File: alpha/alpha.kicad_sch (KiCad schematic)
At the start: 2 parts, among them M1 Motor_AC_3_phase

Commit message: add power circuitry
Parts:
- added C1: 2200uF, 50V, symbol Device:C
- added J1, J2: Conn_01x02, symbol Connector_Generic:Conn_01x02
- added J10, J3, J4, J5, J6, J7, J8, J9: Conn_01x03, symbol Connector_Generic:Conn_01x03
- added M2, M3, M4: Motor_AC_3_phase, symbol Motors:Motor_AC_3_phase
- added U1: Holybro Pixhawk 6X, symbol Flight_Controllers:Holybro_Pixhawk_6X
- added U2: Holybro PM08D Power Module, symbol Power_Modules:Holybro_PM08D_Power_Module
- added U3: Holybro Tekko32 F4 Metal 4in1 65A ESC, symbol ESCs:Tekko32_F4_Metal_4in1_65A_ESC
- added U4: iFlight Anti Spark Filter, symbol Misc:iFlight_Anti_Spark_Filter
- added U5: RFD868x, symbol RF_Modules:RFD868x-EU_868Mhz_Long_Range
- BT1: value Battery -> Battery 6S
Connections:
- net at BT1.1 (+): now also J1.1 (Pin_1)
- net at BT1.2 (-): now also J1.2 (Pin_2)
- net at M1.1: now also J7.1 (Pin_1)
- net at M1.2: now also J7.2 (Pin_2)
- net at M1.3: now also J7.3 (Pin_3)
- new net: J5.1 (Pin_1), U3. (VBAT)
- new net: J5.2 (Pin_2), U3. (VBAT)
- new net: J5.3 (Pin_3), U3. (VBAT)
- new net: J9.1 (Pin_1), M3.1
- new net: J9.2 (Pin_2), M3.2
- new net: J9.3 (Pin_3), M3.3
- new net: U1. (USB-C), U2. (POWER2) (x2)
- new net: J8.1 (Pin_1), M2.1
- new net: J8.2 (Pin_2), M2.2
- new net: J8.3 (Pin_3), M2.3
- new net: C1.1, U2. (POWER2), U3. (VBAT)
- new net: C1.2, U2. (POWER2), U3. (VBAT)
- new net: J2.2 (Pin_2), U4. (V+)
- new net: U2. (POWER2), U4. (V+)
- new net: J10.1 (Pin_1), M4.1
- new net: J10.2 (Pin_2), M4.2
- new net: J10.3 (Pin_3), M4.3
- new net: J3.1 (Pin_1), U3. (VBAT)
- new net: J3.2 (Pin_2), U3. (VBAT)
- new net: J3.3 (Pin_3), U3. (VBAT)
- new net: J4.1 (Pin_1), U3. (VBAT)
- new net: J4.2 (Pin_2), U3. (VBAT)
- new net: J4.3 (Pin_3), U3. (VBAT)
- new net: J6.1 (Pin_1), U3. (VBAT)
- new net: J6.2 (Pin_2), U3. (VBAT)
- new net: J6.3 (Pin_3), U3. (VBAT)
- new net ESC_TEL: U1. (USB-C), U3. (VBAT)
- new net PWM_MOTORS: U1. (USB-C), U3. (VBAT)
- no-connect marks 0 -> 2
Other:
- note added: "18 AWG"
- note added: "6 AWG"
- note added: "AS150"
- note added: "ESC"
- note added: "FUSE 200A"
- note added: "Flight controller"
- note added: "MT30-MAMASS"
- note added: "POWER1 has I2C sensor output"
- note added: "Redundant supply"
- moved on the sheet: BT1

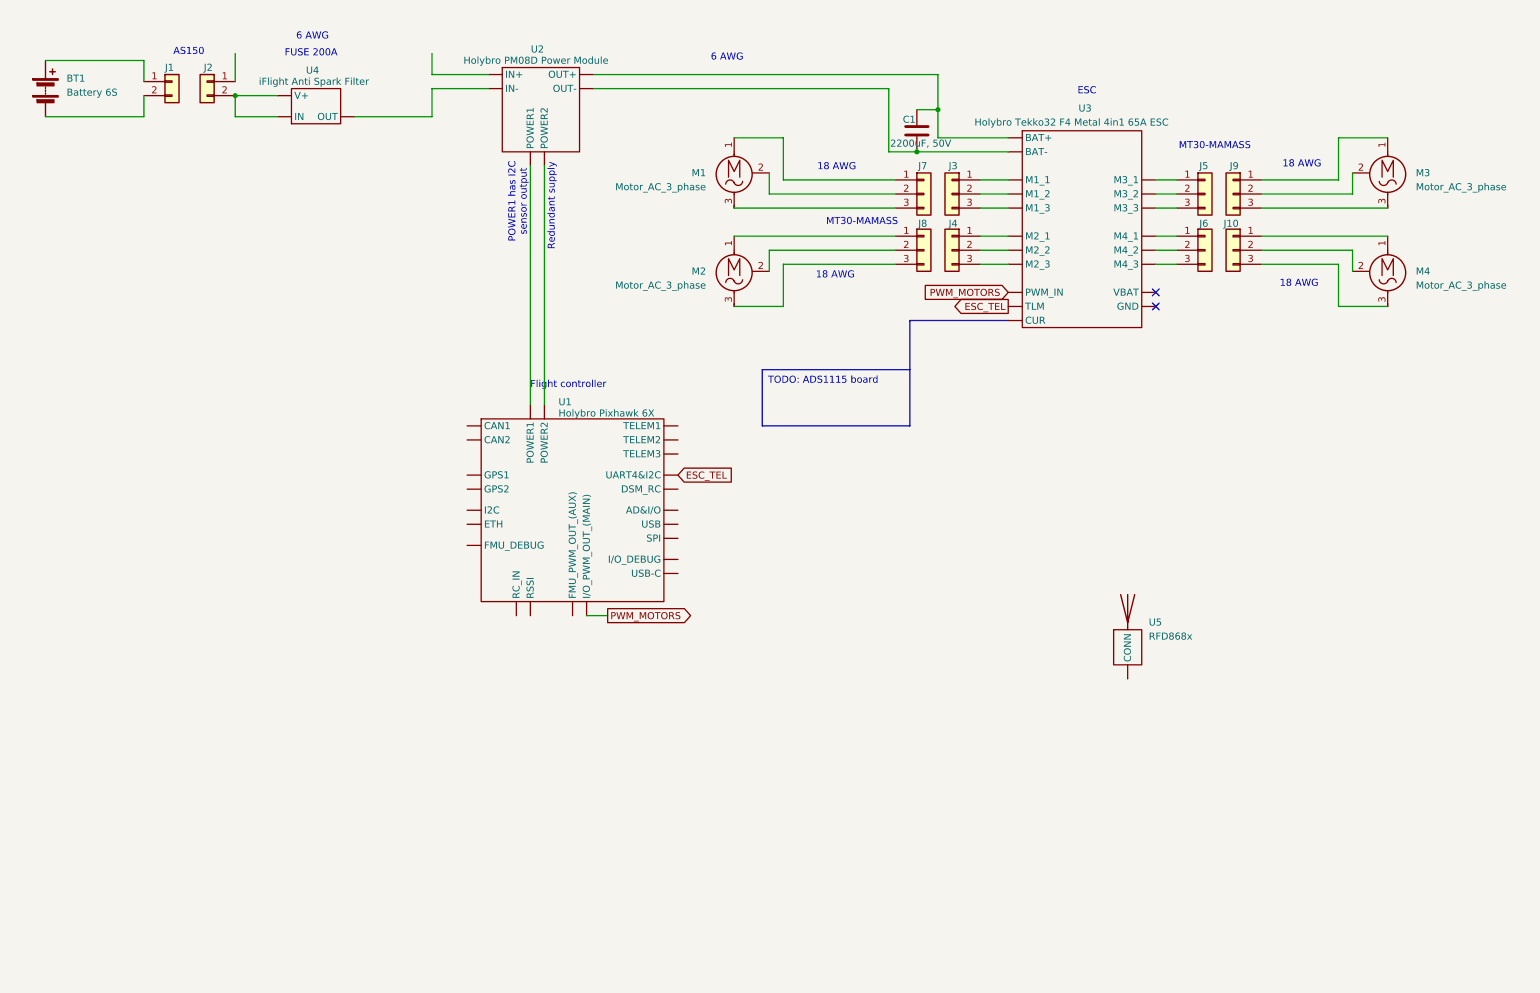
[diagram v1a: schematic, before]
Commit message: Add missing components to schematic
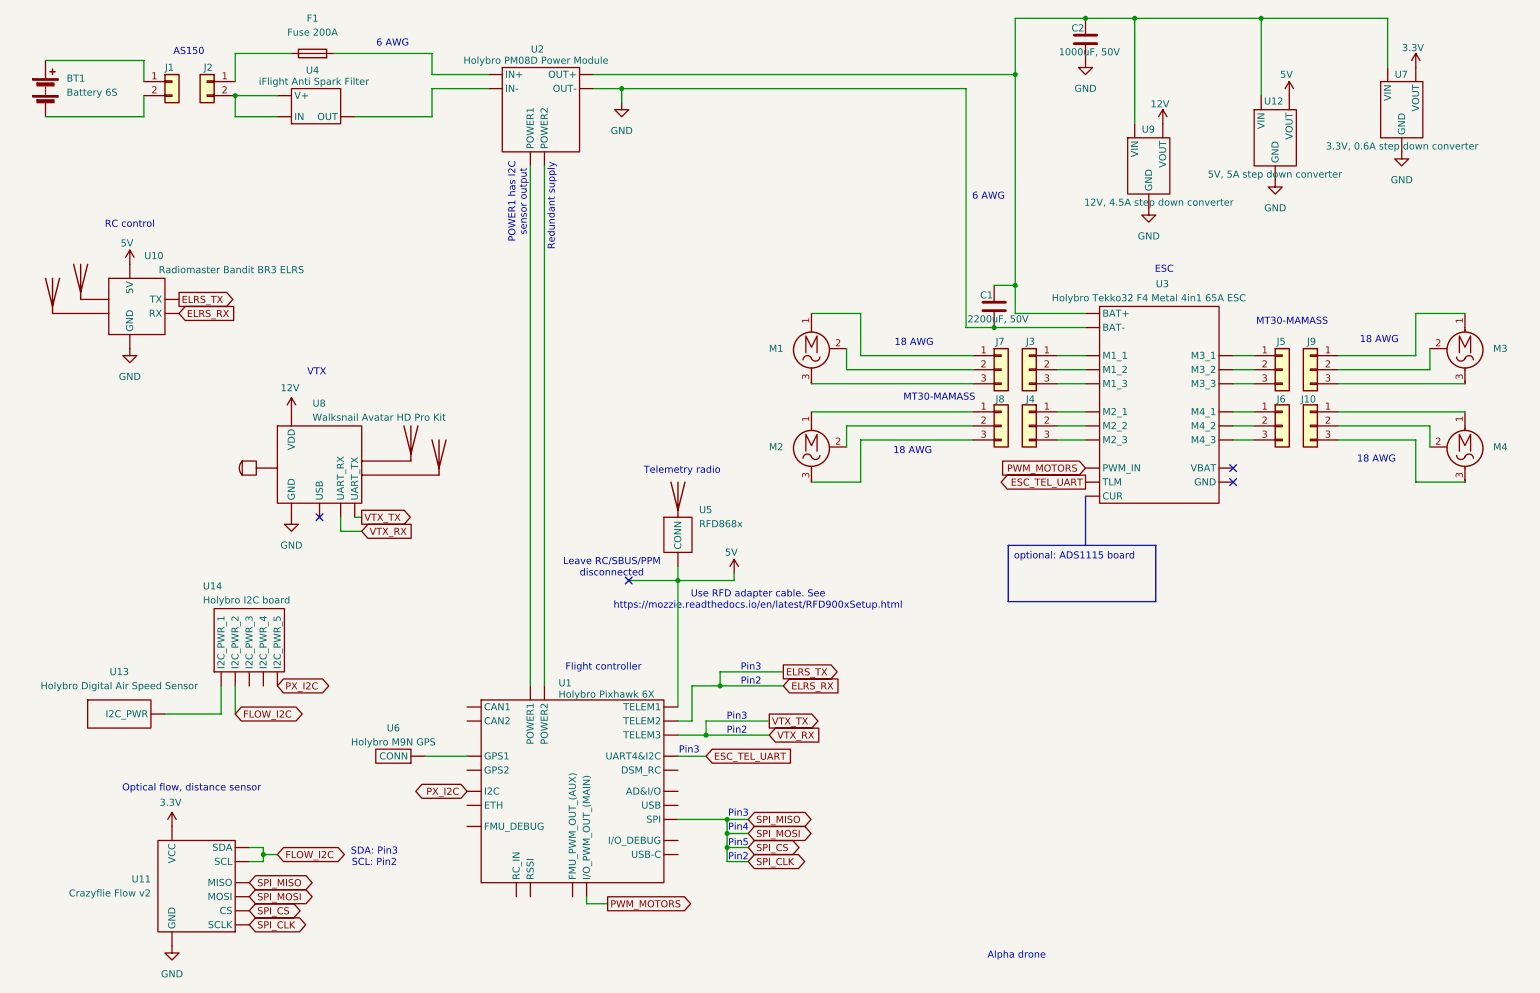
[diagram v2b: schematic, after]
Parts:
- added C2: 1000uF, 50V, symbol Device:C
- added F1: Fuse 200A, symbol Device:Fuse
- added U10: Radiomaster Bandit BR3 ELRS, symbol RF_Modules:Radiomaster_Bandit_BR3_ELRS
- added U11: Crazyflie Flow v2, symbol Sensors:Crazyflie_Flow_v2
- added U12: 5V, 5A step down converter, symbol DC_DC_Converters:DC/DC_Converter
- added U13: Holybro Digital Air Speed Sensor, symbol Sensors:Holybro_Digital_Air_Speed_Sensor
- added U14: Holybro I2C board, symbol Misc:Holybro_I2C_Board
- added U6: Holybro M9N GPS, symbol GPS_Modules:Holybro_M9N_GPS
- added U7: 3.3V, 0.6A step down converter, symbol DC_DC_Converters:DC/DC_Converter
- added U8: Walksnail Avatar HD Pro Kit, symbol Camera_VTX:Walksnail_Avatar_HD_Pro_Kit
- added U9: 12V, 4.5A step down converter, symbol DC_DC_Converters:DC/DC_Converter
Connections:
- net VTX_RX: now reaches U1. (USB-C)
- net VTX_RX: now also U8. (VDD)
- net GND: now reaches U2. (POWER2)
- net GND: now also C1.2, U3. (VBAT), C2.2, U10. (TX), U11. (VCC), U12. (VOUT), U7. (VOUT), U8. (VDD), U9. (VOUT); no longer U1. (USB-C)
- net at J2.1 (Pin_1): now also F1.1
- net 5V: now reaches U5. (CONN)
- net 5V: now also U1. (USB-C), U10. (TX), U12. (VOUT)
- removed net ESC_TEL: U1. (USB-C), U3. (VBAT)
- new net: U1. (USB-C), U2. (POWER2) (x2)
- new net: U1. (USB-C), U6. (CONN)
- new net: C1.1, C2.1, U12. (VOUT), U2. (POWER2), U3. (VBAT), U7. (VOUT), U9. (VOUT)
- new net: U13. (I2C_PWR), U14. (I2C_PWR_5)
- new net: F1.2, U2. (POWER2)
- new net 12V: U8. (VDD), U9. (VOUT)
- new net 3.3V: U11. (VCC), U7. (VOUT)
- new net ELRS_RX: U1. (USB-C), U10. (TX)
- new net ESC_TEL_UART: U1. (USB-C), U3. (VBAT)
- new net FLOW_I2C: U11. (VCC), U14. (I2C_PWR_5)
- new net PX_I2C: U1. (USB-C), U14. (I2C_PWR_5)
- new net SPI_CLK: U1. (USB-C), U11. (VCC)
- no-connect marks 2 -> 4
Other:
- note added: "Alpha drone"
- note added: "Leave RC/SBUS/PPM disconnected"
- note added: "Optical flow, distance sensor"
- note added: "Pin2"
- note added: "Pin3"
- note added: "Pin4"
- note added: "Pin5"
- note added: "RC control"
- note added: "SDA: Pin3 SCL: Pin2"
- note added: "Telemetry radio"
- note added: "Use RFD adapter cable. See https://mozzie.readthedocs.io/en/latest/RFD900xSetup.html"
- note added: "VTX"
- note removed: "FUSE 200A"
- moved on the sheet: C1, J10, J3, J4, J5, J6, J7, J8, J9, M1, M2, M3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

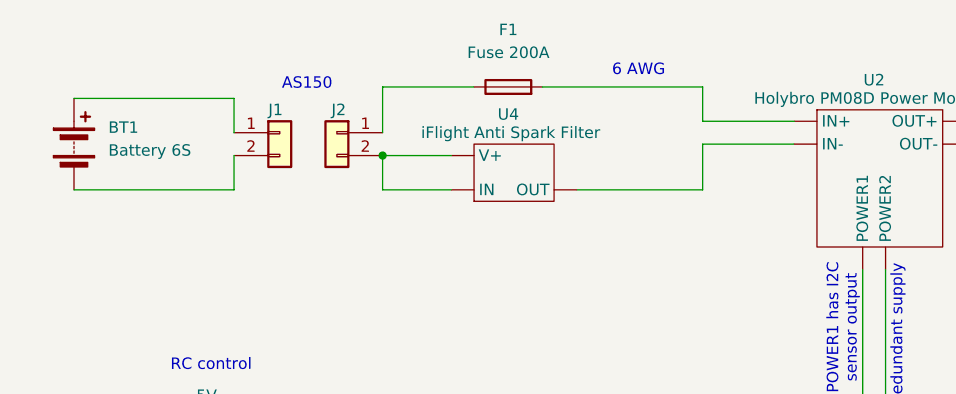
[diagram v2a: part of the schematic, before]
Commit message: fix anti spark filter
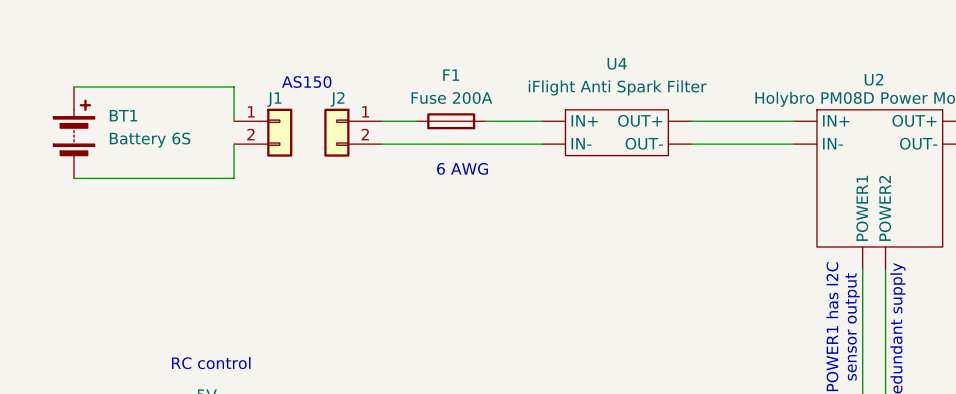
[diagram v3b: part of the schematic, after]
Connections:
- net at U4. (OUT-): now also F1.2; no longer U2. (POWER2)
- new net: U1. (USB-C), U2. (POWER2) (x2)
- new net: C1.1, C2.1, U12. (VOUT), U2. (POWER2), U3. (VBAT), U7. (VOUT), U9. (VOUT)
- new net: U2. (POWER2), U4. (OUT-) (x2)
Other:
- moved on the sheet: BT1, F1, J1, J2

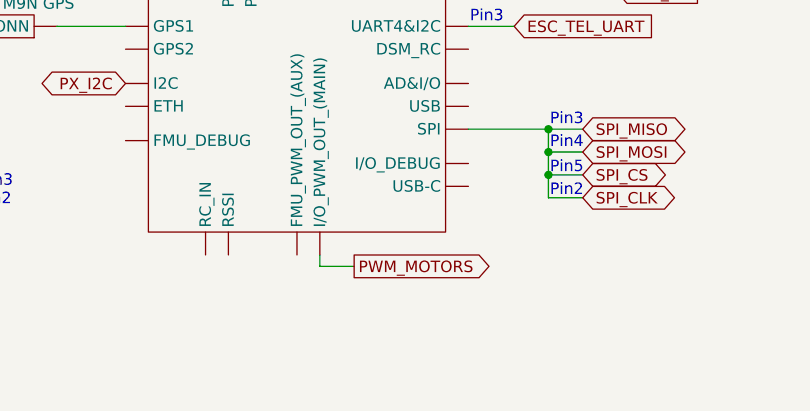
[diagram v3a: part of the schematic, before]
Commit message: assign motors to ports supporting dshot
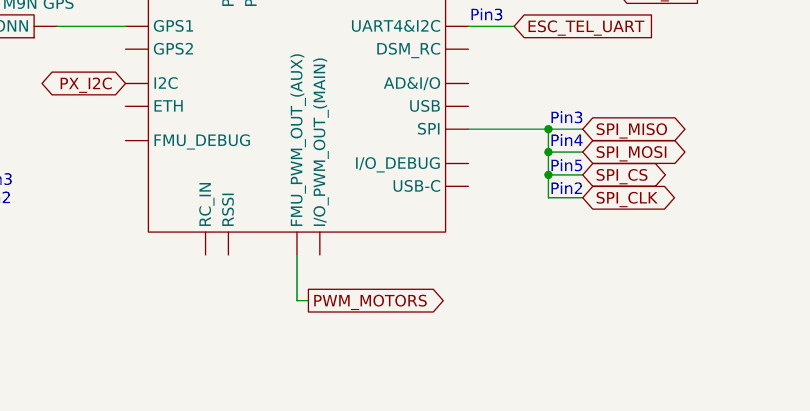
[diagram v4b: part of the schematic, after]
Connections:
- net at U4. (OUT-): now also F1.2; no longer U2. (POWER2)
- new net: U1. (USB-C), U2. (POWER2) (x2)
- new net: C1.1, C2.1, U12. (VOUT), U2. (POWER2), U3. (VBAT), U7. (VOUT), U9. (VOUT)
- new net: U2. (POWER2), U4. (OUT-) (x2)
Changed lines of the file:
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@@
 	(wire
 		(pts
-			(xy 119.38 180.34) (xy 115.57 180.34)
+			(xy 114.3 184.15) (xy 113.03 184.15)
 		)
 		(stroke
@@
 	(wire
 		(pts
-			(xy 115.57 180.34) (xy 115.57 179.07)
+			(xy 113.03 184.15) (xy 113.03 179.07)
 		)
 		(stroke
@@
 	(global_label "PWM_MOTORS"
 		(shape output)
-		(at 119.38 180.34 0)
+		(at 114.3 184.15 0)
 		(fields_autoplaced yes)
 		(effects
@@
 		)
 		(property "Intersheetrefs" "${INTERSHEET_REFS}"
-			(at 135.0651 180.34 0)
+			(at 129.9851 184.15 0)
 			(effects
 				(font

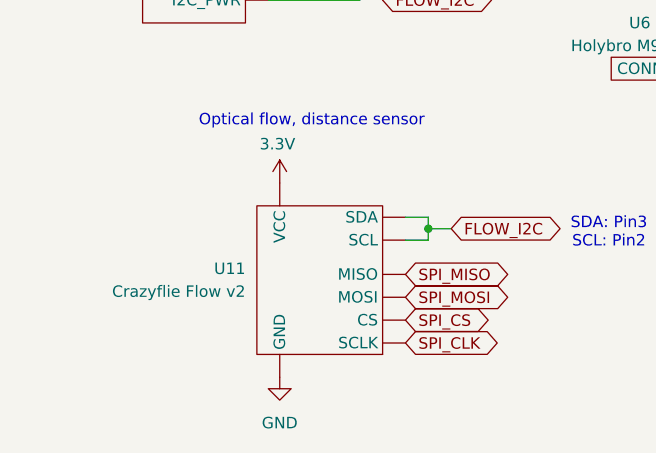
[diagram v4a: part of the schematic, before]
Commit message: fix optical flow sensor wiring
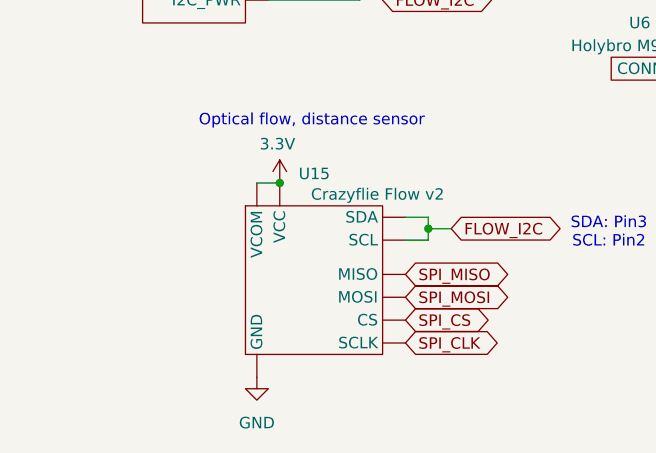
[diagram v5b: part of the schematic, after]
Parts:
- removed U11: Crazyflie Flow v2, symbol Sensors:Crazyflie_Flow_v2
- added U15: Crazyflie Flow v2, symbol Sensors:Crazyflie_Flow_v2
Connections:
- net 3.3V: now also U15. (VCOM)
- net FLOW_I2C: now also U15. (VCOM)
- net GND: now also U15. (VCOM)
- net SPI_CLK: now also U15. (VCOM)
- net at U4. (OUT-): now also F1.2; no longer U2. (POWER2)
- new net: U1. (USB-C), U2. (POWER2) (x2)
- new net: C1.1, C2.1, U12. (VOUT), U2. (POWER2), U3. (VBAT), U7. (VOUT), U9. (VOUT)
- new net: U2. (POWER2), U4. (OUT-) (x2)
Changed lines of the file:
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@@
 	)
 	(junction
+		(at 40.64 166.37)
+		(diameter 0)
+		(color 0 0 0 0)
+	)
+	(junction
 		(at 214.63 20.32)
 		(diameter 0)
@@
 	(wire
 		(pts
+			(xy 38.1 166.37) (xy 40.64 166.37)
+		)
+		(stroke
+			(width 0)
+			(type default)
+		)
+	)
+	(wire
+		(pts
 			(xy 142.24 121.92) (xy 142.24 120.65)
 		)
@@
 	(symbol
 		(lib_id "power:GND")
-		(at 40.64 187.96 0)
+		(at 38.1 187.96 0)
 		(unit 1)
 		(exclude_from_sim no)
@@
 		(fields_autoplaced yes)
 		(property "Reference" "#PWR015"
-			(at 40.64 194.31 0)
+			(at 38.1 194.31 0)
 			(effects
 				(font
@@
 		)
 		(property "Value" "GND"
-			(at 40.64 193.04 0)
+			(at 38.1 193.04 0)
 			(effects
 				(font
@@
 		)
 		(property "Footprint" ""
-			(at 40.64 187.96 0)
+			(at 38.1 187.96 0)
 			(effects
 				(font
@@
 		)
 		(property "Datasheet" ""
-			(at 40.64 187.96 0)
+			(at 38.1 187.96 0)
 			(effects
 				(font
@@
 		)
 		(property "Description" "Power symbol creates a global label with name \"GND\" , ground"
-			(at 40.64 187.96 0)
+			(at 38.1 187.96 0)
 			(effects
 				(font
@@
 	)
 	(symbol
-		(lib_id "power:GND")
-		(at 121.92 35.56 0)
+		(lib_name "Crazyflie_Flow_v2_1")
+		(lib_id "Sensors:Crazyflie_Flow_v2")
+		(at 45.72 175.26 0)
 		(unit 1)
 		(exclude_from_sim no)
@@
 		(on_board yes)
 		(dnp no)
-		(fields_autoplaced yes)
-		(property "Reference" "#PWR01"
-			(at 121.92 41.91 0)
+		(property "Reference" "U15"
+			(at 46.228 165.354 0)
 			(effects
 				(font
 					(size 1.27 1.27)
 				)
-				(hide yes)
+				(justify right)
 			)
 		)
-		(property "Value" "GND"
-			(at 121.92 40.64 0)
+		(property "Value" "Crazyflie Flow v2"
+			(at 58.928 167.64 0)
 			(effects
 				(font
 					(size 1.27 1.27)
 				)
+				(justify right)
 			)
 		)
 		(property "Footprint" ""
-			(at 121.92 35.56 0)
+			(at 71.12 175.26 0)
 			(effects
 				(font
@@
 		)
 		(property "Datasheet" ""
-			(at 121.92 35.56 0)
+			(at 71.12 175.26 0)
 			(effects
 				(font
@@
 			)
 		)
-		(property "Description" "Power symbol creates a global label with name \"GND\" , ground"
-			(at 121.92 35.56 0)
+		(property "Description" ""
+			(at 71.12 175.26 0)
 			(effects
 				(font
@@
 			)
 		)
-		(pin "1"
+		(pin ""
+		)
+		(pin ""
+		)
+		(pin ""
+		)
+		(pin ""
+		)
+		(pin ""
+		)
+		(pin ""
+		)
+		(pin ""
+		)
+		(pin ""
+		)
+		(pin ""
 		)
 		(instances
 			(project ""
 				(path "/e82fdf23-e984-4547-bc35-f76b36d3e186"
-					(reference "#PWR01")
+					(reference "U15")
 					(unit 1)
 				)
@@
 	)
 	(symbol
-		(lib_id "power:+12V")
-		(at 33.02 64.77 0)
+		(lib_id "power:GND")
+		(at 121.92 35.56 0)
 		(unit 1)
 		(exclude_from_sim no)
@@
 		(on_board yes)
 		(dnp no)
-		(property "Reference" "#PWR011"
-			(at 33.02 68.58 0)
+		(fields_autoplaced yes)
+		(property "Reference" "#PWR01"
+			(at 121.92 41.91 0)
 			(effects
 				(font
@@
 			)
 		)
-		(property "Value" "5V"
-			(at 32.512 60.96 0)
+		(property "Value" "GND"
+			(at 121.92 40.64 0)
 			(effects
 				(font
@@
 		)
 		(property "Footprint" ""
-			(at 33.02 64.77 0)
+			(at 121.92 35.56 0)
 			(effects
 				(font
@@
 		)
 		(property "Datasheet" ""
-			(at 33.02 64.77 0)
+			(at 121.92 35.56 0)
 			(effects
 				(font
@@
 			)
 		)
-		(property "Description" "Power symbol creates a global label with name \"+12V\""
-			(at 33.02 64.77 0)
+		(property "Description" "Power symbol creates a global label with name \"GND\" , ground"
+			(at 121.92 35.56 0)
 			(effects
 				(font
@@
 		)
 		(instances
-			(project "alpha"
+			(project ""
 				(path "/e82fdf23-e984-4547-bc35-f76b36d3e186"
-					(reference "#PWR011")
+					(reference "#PWR01")
 					(unit 1)
 				)
@@
 	)
 	(symbol
-		(lib_id "power:GND")
-		(at 33.02 80.01 0)
+		(lib_id "power:+12V")
+		(at 33.02 64.77 0)
 		(unit 1)
 		(exclude_from_sim no)
@@
 		(on_board yes)
 		(dnp no)
-		(fields_autoplaced yes)
-		(property "Reference" "#PWR010"
-			(at 33.02 86.36 0)
+		(property "Reference" "#PWR011"
+			(at 33.02 68.58 0)
 			(effects
 				(font
@@
 			)
 		)
-		(property "Value" "GND"
-			(at 33.02 85.09 0)
+		(property "Value" "5V"
+			(at 32.512 60.96 0)
 			(effects
 				(font
@@
 		)
 		(property "Footprint" ""
-			(at 33.02 80.01 0)
+			(at 33.02 64.77 0)
 			(effects
 				(font
@@
 		)
 		(property "Datasheet" ""
-			(at 33.02 80.01 0)
+			(at 33.02 64.77 0)
 			(effects
 				(font
@@
 			)
 		)
-		(property "Description" "Power symbol creates a global label with name \"GND\" , ground"
-			(at 33.02 80.01 0)
+		(property "Description" "Power symbol creates a global label with name \"+12V\""
+			(at 33.02 64.77 0)
 			(effects
 				(font
@@
 			(project "alpha"
 				(path "/e82fdf23-e984-4547-bc35-f76b36d3e186"
-					(reference "#PWR010")
+					(reference "#PWR011")
 					(unit 1)
 				)
@@
 	)
 	(symbol
-		(lib_id "Sensors:Crazyflie_Flow_v2")
-		(at 45.72 175.26 0)
+		(lib_id "power:GND")
+		(at 33.02 80.01 0)
 		(unit 1)
 		(exclude_from_sim no)
@@
 		(dnp no)
 		(fields_autoplaced yes)
-		(property "Reference" "U11"
-			(at 36.83 175.8949 0)
+		(property "Reference" "#PWR010"
+			(at 33.02 86.36 0)
 			(effects
 				(font
 					(size 1.27 1.27)
 				)
-				(justify right)
+				(hide yes)
 			)
 		)
-		(property "Value" "Crazyflie Flow v2"
-			(at 36.83 178.4349 0)
+		(property "Value" "GND"
+			(at 33.02 85.09 0)
 			(effects
 				(font
 					(size 1.27 1.27)
 				)
-				(justify right)
 			)
 		)
 		(property "Footprint" ""
-			(at 71.12 175.26 0)
+			(at 33.02 80.01 0)
 			(effects
 				(font
@@
 		)
 		(property "Datasheet" ""
-			(at 71.12 175.26 0)
+			(at 33.02 80.01 0)
 			(effects
 				(font
@@
 			)
 		)
-		(property "Description" ""
-			(at 71.12 175.26 0)
+		(property "Description" "Power symbol creates a global label with name \"GND\" , ground"
+			(at 33.02 80.01 0)
 			(effects
 				(font
@@
 			)
 		)
-		(pin ""
-		)
-		(pin ""
-		)
-		(pin ""
-		)
-		(pin ""
-		)
-		(pin ""
-		)
-		(pin ""
-		)
-		(pin ""
-		)
-		(pin ""
+		(pin "1"
 		)
 		(instances
-			(project ""
+			(project "alpha"
 				(path "/e82fdf23-e984-4547-bc35-f76b36d3e186"
-					(reference "U11")
+					(reference "#PWR010")
 					(unit 1)
 				)
